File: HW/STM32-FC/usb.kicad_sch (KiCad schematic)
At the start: 15 parts, among them J3 USB_C_Receptacle_USB2.0_14P, SW1 SW_DIP_x01, U2 AMS1117-3.3, U3 AMS1117-3.3, U4 USBLC6-2SC6

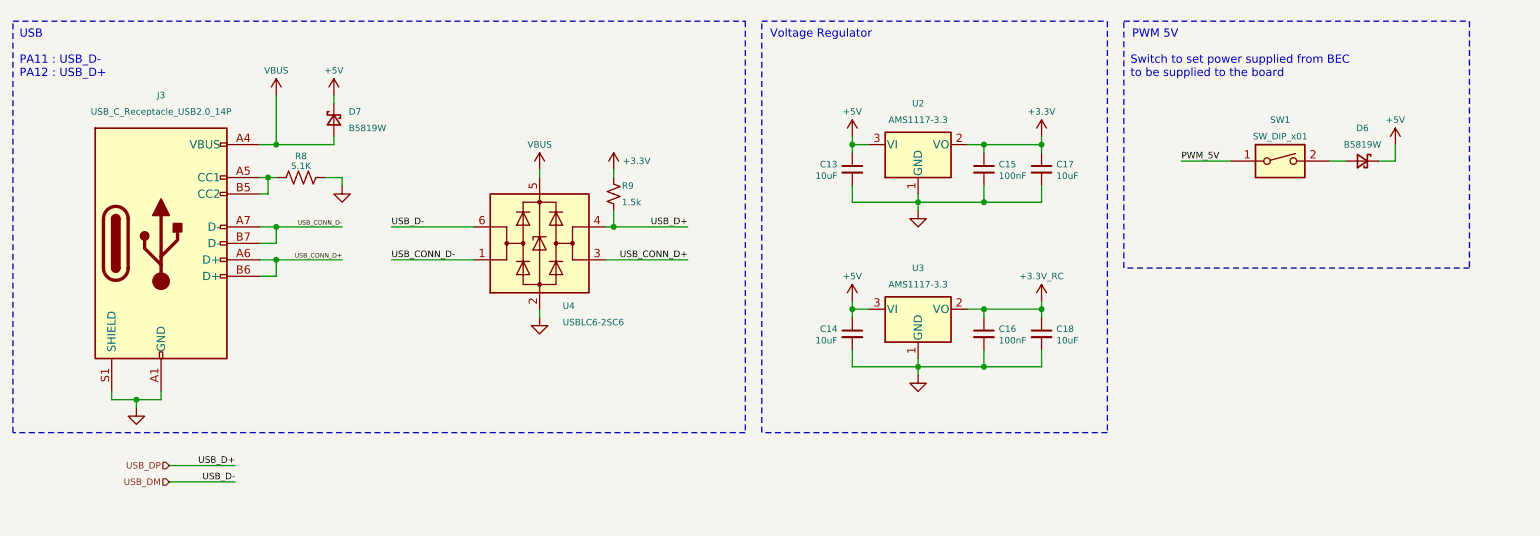
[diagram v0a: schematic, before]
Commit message: 2025.01.03v2:PM(Power Module) added
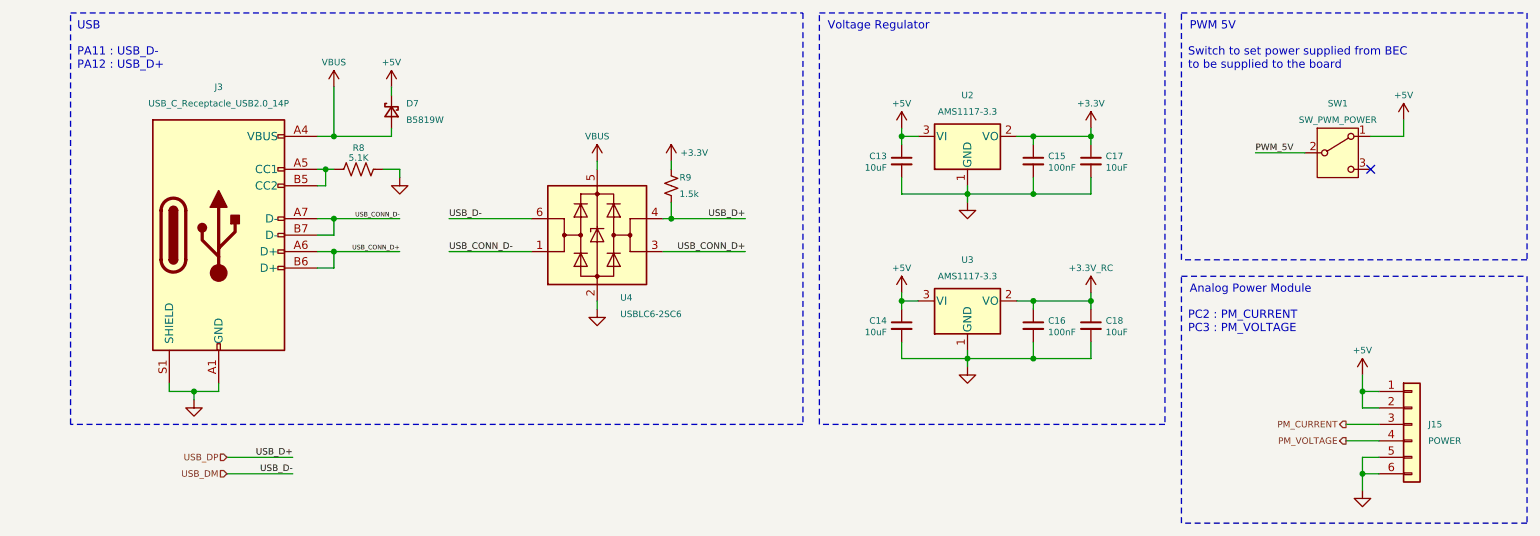
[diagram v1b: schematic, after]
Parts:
- removed D6: B5819W, Diode_SMD:D_SOD-123, symbol Device:D_Schottky_Small
- added J15: POWER, Connectors_JST:JST_GH_BM06B-GHS-TBT_06x1.25mm_Straight, symbol Connector_Generic:Conn_01x06
- SW1: value SW_DIP_x01 -> SW_PWM_POWER; symbol Switch:SW_DIP_x01 -> Switch:SW_SPDT
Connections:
- net +5V: now also SW1.1 (A), J15.1 (Pin_1), J15.2 (Pin_2)
- net GND: now also J15.5 (Pin_5), J15.6 (Pin_6)
- net PWM_5V: now also SW1.2 (B); no longer SW1.1
- new net PM_CURRENT: J15.3 (Pin_3)
- new net PM_VOLTAGE: J15.4 (Pin_4)
- no-connect marks 0 -> 1
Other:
- note added: "Analog Power Module"
- note added: "PC2 : PM_CURRENT PC3 : PM_VOLTAGE"
- company: INHA UNIV. NARAE -> NARAE
- moved on the sheet: C13, C14, C15, C16, C17, C18, D7, J3, R8, R9, U2, U3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

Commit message: Baro/SD Card update
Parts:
- removed D7: B5819W, Diode_SMD:D_SOD-123, symbol Device:D_Schottky_Small
- removed U2: AMS1117-3.3, Package_TO_SOT_SMD:SOT-223-3_TabPin2, symbol Regulator_Linear:AMS1117-3.3
- added D6: B5819W, Diode_SMD:D_SOD-123, symbol Device:D_Schottky_Small
- added U4: AMS1117-3.3, Package_TO_SOT_SMD:SOT-89-3, symbol Regulator_Linear:AMS1117-3.3
- J4: renamed from J3; value USB_C_Receptacle_USB2.0_14P -> USB_C_USB2.0_14P; footprint Connector_USB:USB_C_Receptacle_Amphenol_12401548E4-2A -> Connector_USB:USB_C_Receptacle_GCT_USB4110
- J5: renamed from J15; value POWER -> GH 1.25mm 6P; footprint Connectors_JST:JST_GH_BM06B-GHS-TBT_06x1.25mm_Straight -> JST_GH:JST_GH_BM06B-GHS-TBT_06
- R8: value 5.1K -> 5k1
- R9: value 1.5k -> 1k5
- SW1: value SW_PWM_POWER -> SK-02; footprint (none) -> SK-02:SK-02
- U3: footprint Package_TO_SOT_SMD:SOT-223-3_TabPin2 -> Package_TO_SOT_SMD:SOT-89-3; LCSC C6186 -> (none)
- renumbered U4 to U2
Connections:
- net +3.3V: now also U3.2 (VO)
- net +3.3V_RC: now also U4.2 (VO); no longer U3.2 (VO)
- net +5V: now also D6.1 (K), U4.3 (VI)
- net GND: now also U4.1 (GND)
- net VBUS: now also D6.2 (A)
- net PWM_5V renamed +5V_PWM
- net USB_DM renamed USB_D-
- net USB_DP renamed USB_D+
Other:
- note added: "GH 1.25mm 6P PC2 : PM_CURRENT PC3 : PM_VOLTAGE"
- note removed: "PC2 : PM_CURRENT PC3 : PM_VOLTAGE"

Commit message: 2025.01.16
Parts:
- D6: footprint Diode_SMD:D_SOD-123 -> Diode_SMD:D_SOD-323
- renumbered C15 to C14, C17 to C15, C14 to C16, C16 to C17, U3 to U2, U2 to U3

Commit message: 2025.01.17 : PCB layout
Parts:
- removed SW1: SK-02, SK-02:SK-02, symbol Switch:SW_SPDT
- renumbered C16 to C14, C14 to C15, C17 to C16, C15 to C17, J4 to J2, J5 to J3, R9 to R10, R8 to R9, U3 to U2, U2 to U3
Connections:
- no-connect marks 1 -> 0
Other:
- note removed: "PWM 5V"
- note removed: "Switch to set power supplied from BEC to be supplied to the board"
- moved on the sheet: J3

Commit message: 2025.02.06 PCB routing done v2
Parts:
- C13, C14, C17, C18: LCSC (none) -> C40894
- C15, C16: LCSC (none) -> C1581
- D6: LCSC C8598 -> C22624
- J2: LCSC (none) -> C5143397
- J3: LCSC (none) -> C189892
- R10: LCSC (none) -> C25867
- R9: LCSC (none) -> C25905
- U2: LCSC (none) -> C7519
- U3, U4: LCSC (none) -> C22472154
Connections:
- net +5V: now also J3.5 (Pin_5), J3.6 (Pin_6); no longer J3.1 (Pin_1), J3.2 (Pin_2)
- net GND: now also J3.1 (Pin_1), J3.2 (Pin_2); no longer J3.5 (Pin_5), J3.6 (Pin_6)
- net PM_CURRENT: now also J3.4 (Pin_4); no longer J3.3 (Pin_3)
- net PM_VOLTAGE: now also J3.3 (Pin_3); no longer J3.4 (Pin_4)
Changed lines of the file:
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@@
 			)
 		)
+		(property "LCSC" "C1581"
+			(at 171.45 35.56 0)
+			(effects
+				(font
+					(size 1.27 1.27)
+				)
+				(hide yes)
+			)
+		)
 		(pin "1"
 		)
@@
 			)
 		)
+		(property "LCSC" "C40894"
+			(at 180.34 60.96 0)
+			(effects
+				(font
+					(size 1.27 1.27)
+				)
+				(hide yes)
+			)
+		)
 		(pin "1"
 		)
@@
 	(symbol
 		(lib_id "Connector_Generic:Conn_01x06")
-		(at 229.87 35.56 0)
+		(at 229.87 38.1 0)
+		(mirror x)
 		(unit 1)
 		(exclude_from_sim no)
@@
 		(on_board yes)
 		(dnp no)
-		(fields_autoplaced yes)
 		(property "Reference" "J3"
-			(at 232.41 35.56 0)
+			(at 232.41 38.1 0)
 			(effects
 				(font
@@
 		)
 		(property "Value" "GH 1.25mm 6P"
-			(at 232.41 38.1 0)
+			(at 232.41 35.56 0)
 			(effects
 				(font
@@
 		)
 		(property "Footprint" "JST_GH:JST_GH_BM06B-GHS-TBT_06"
-			(at 229.87 35.56 0)
+			(at 229.87 38.1 0)
 			(effects
 				(font
@@
 		)
 		(property "Datasheet" "~"
-			(at 229.87 35.56 0)
+			(at 229.87 38.1 0)
 			(effects
 				(font
@@
 		)
 		(property "Description" "Generic connector, single row, 01x06, script generated (kicad-library-utils/schlib/autogen/connector/)"
-			(at 229.87 35.56 0)
+			(at 229.87 38.1 0)
 			(effects
 				(font
@@
 		)
 		(property "Availability" ""
-			(at 229.87 35.56 0)
+			(at 229.87 38.1 0)
 			(effects
 				(font
@@
 		)
 		(property "Check_prices" ""
-			(at 229.87 35.56 0)
+			(at 229.87 38.1 0)
 			(effects
 				(font
@@
 		)
 		(property "Description_1" ""
-			(at 229.87 35.56 0)
+			(at 229.87 38.1 0)
 			(effects
 				(font
@@
 		)
 		(property "MF" ""
-			(at 229.87 35.56 0)
+			(at 229.87 38.1 0)
 			(effects
 				(font
@@
 		)
 		(property "MP" ""
-			(at 229.87 35.56 0)
+			(at 229.87 38.1 0)
 			(effects
 				(font
@@
 		)
 		(property "Package" ""
-			(at 229.87 35.56 0)
+			(at 229.87 38.1 0)
 			(effects
 				(font
@@
 		)
 		(property "Price" ""
-			(at 229.87 35.56 0)
+			(at 229.87 38.1 0)
 			(effects
 				(font
@@
 		)
 		(property "SnapEDA_Link" ""
-			(at 229.87 35.56 0)
+			(at 229.87 38.1 0)
 			(effects
 				(font
@@
 		)
 		(property "Sim.Device" ""
-			(at 229.87 35.56 0)
+			(at 229.87 38.1 0)
 			(effects
 				(font
@@
 		)
 		(property "Sim.Pins" ""
-			(at 229.87 35.56 0)
+			(at 229.87 38.1 0)
+			(effects
+				(font
+					(size 1.27 1.27)
+				)
+				(hide yes)
+			)
+		)
+		(property "LCSC" "C189892"
+			(at 229.87 38.1 0)
 			(effects
 				(font
@@
 			)
 		)
+		(property "LCSC" "C22472154"
+			(at 161.29 57.15 0)
+			(effects
+				(font
+					(size 1.27 1.27)
+				)
+				(hide yes)
+			)
+		)
 		(pin "1"
 		)
@@
 			)
 		)
+		(property "LCSC" "C40894"
+			(at 151.13 35.56 0)
+			(effects
+				(font
+					(size 1.27 1.27)
+				)
+				(hide yes)
+			)
+		)
 		(pin "1"
 		)
@@
 			)
 		)
+		(property "LCSC" "C1581"
+			(at 171.45 60.96 0)
+			(effects
+				(font
+					(size 1.27 1.27)
+				)
+				(hide yes)
+			)
+		)
 		(pin "1"
 		)
@@
 			)
 		)
-		(property "LCSC" "C8598"
+		(property "LCSC" "C22624"
 			(at 72.39 27.94 90)
 			(effects
@@
 			)
 		)
+		(property "LCSC" "C22472154"
+			(at 161.29 31.75 0)
+			(effects
+				(font
+					(size 1.27 1.27)
+				)
+				(hide yes)
+			)
+		)
 		(pin "2"
 		)
@@
 			)
 		)
+		(property "LCSC" "C7519"
+			(at 104.14 46.99 0)
+			(effects
+				(font
+					(size 1.27 1.27)
+				)
+				(hide yes)
+			)
+		)
 		(pin "1"
 		)
@@
 			)
 		)
+		(property "LCSC" "C40894"
+			(at 180.34 35.56 0)
+			(effects
+				(font
+					(size 1.27 1.27)
+				)
+				(hide yes)
+			)
+		)
 		(pin "1"
 		)
@@
 			)
 		)
+		(property "LCSC" "C40894"
+			(at 151.13 60.96 0)
+			(effects
+				(font
+					(size 1.27 1.27)
+				)
+				(hide yes)
+			)
+		)
 		(pin "1"
 		)
@@
 			)
 		)
+		(property "LCSC" "C25905"
+			(at 67.31 36.83 0)
+			(effects
+				(font
+					(size 1.27 1.27)
+				)
+				(hide yes)
+			)
+		)
 		(pin "2"
 		)
@@
 			)
 		)
+		(property "LCSC" "C5143397"
+			(at 45.72 46.99 0)
+			(effects
+				(font
+					(size 1.27 1.27)
+				)
+				(hide yes)
+			)
+		)
 		(pin "B4"
 		)
@@
 			(at 115.57 39.37 0)
 			(effects
+				(font
+					(size 1.27 1.27)
+				)
+				(hide yes)
+			)
+		)
+		(property "LCSC" "C25867"
+			(at 115.57 39.37 0)
+			(effects
